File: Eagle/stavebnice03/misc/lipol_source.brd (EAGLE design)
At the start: 24 parts

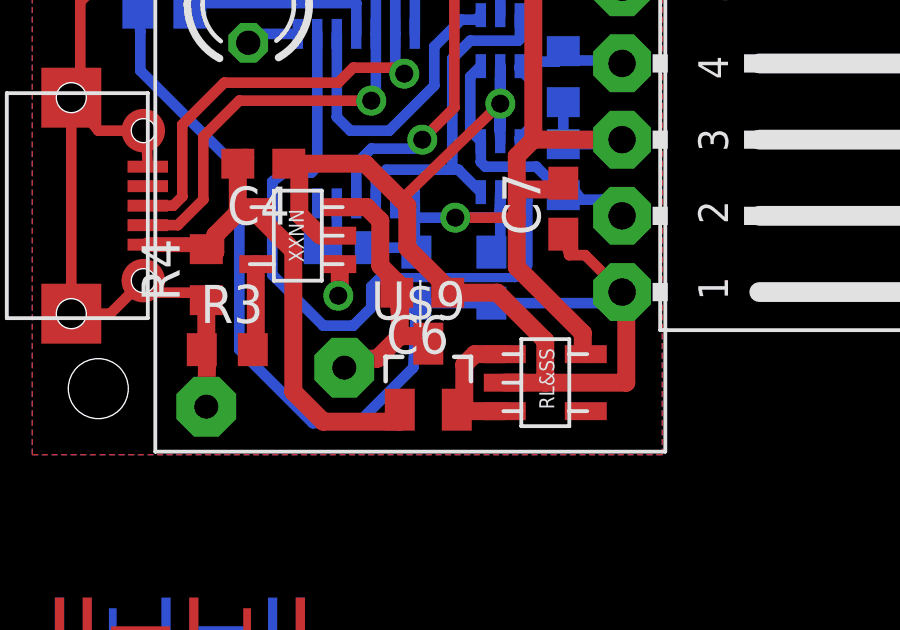
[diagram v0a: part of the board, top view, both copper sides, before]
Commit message: values for lipol charger
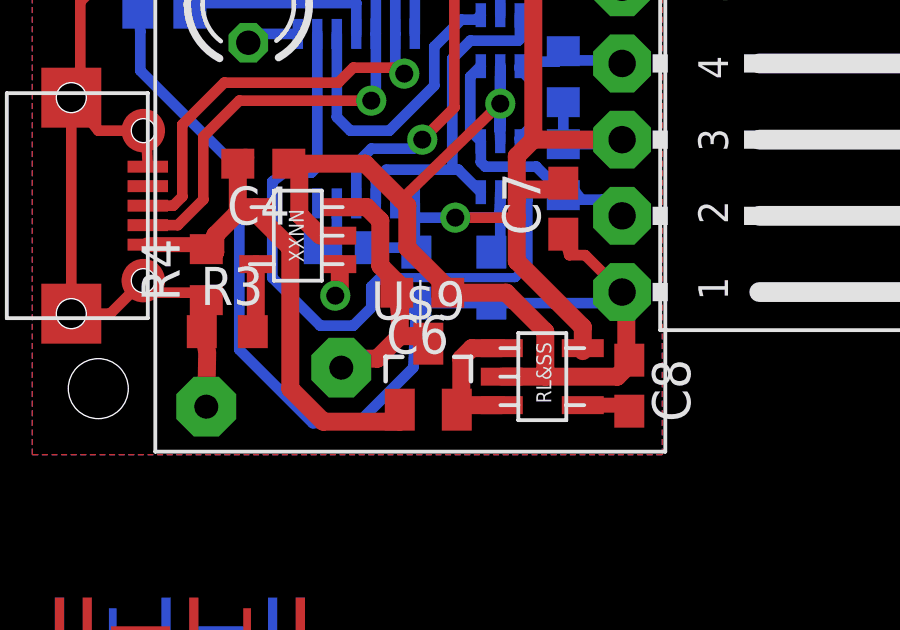
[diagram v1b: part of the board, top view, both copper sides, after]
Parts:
- removed U$8: STABILISER_APE8865, !stavebnice03:SOT32-5
- added C8: 470pF, resistor:C0603
- added TC1185: STABILISER_APE8865, !stavebnice03:SOT32-5
- R3: value 2k2 -> 22k
- R4: value 2k2 -> 100k
- R5: value 0 -> 10k
- R6: value 0 -> 100
- moved R3 0.60 mm to (6.50, 4.10)
- renumbered U$4 to MCP73832, U$6 to NC7SB3157P6X(1), U$7 to NC7SB3157P6X(2)
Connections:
- new net N$17: C8.2, TC1185.BP
- net GND: now also C8.1, TC1185.GND; no longer U$8.GND
- net N$12: now also TC1185.SHDN, TC1185.VIN; no longer U$8.SHDN, U$8.VIN
- net VCC: now also TC1185.VOUT; no longer U$8.VOUT
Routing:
- net N$17: track 0.00 -> 1.75 mm
- net GND: track 138.7 -> 139.3 mm
- net N$11: track 2.89 -> 2.29 mm

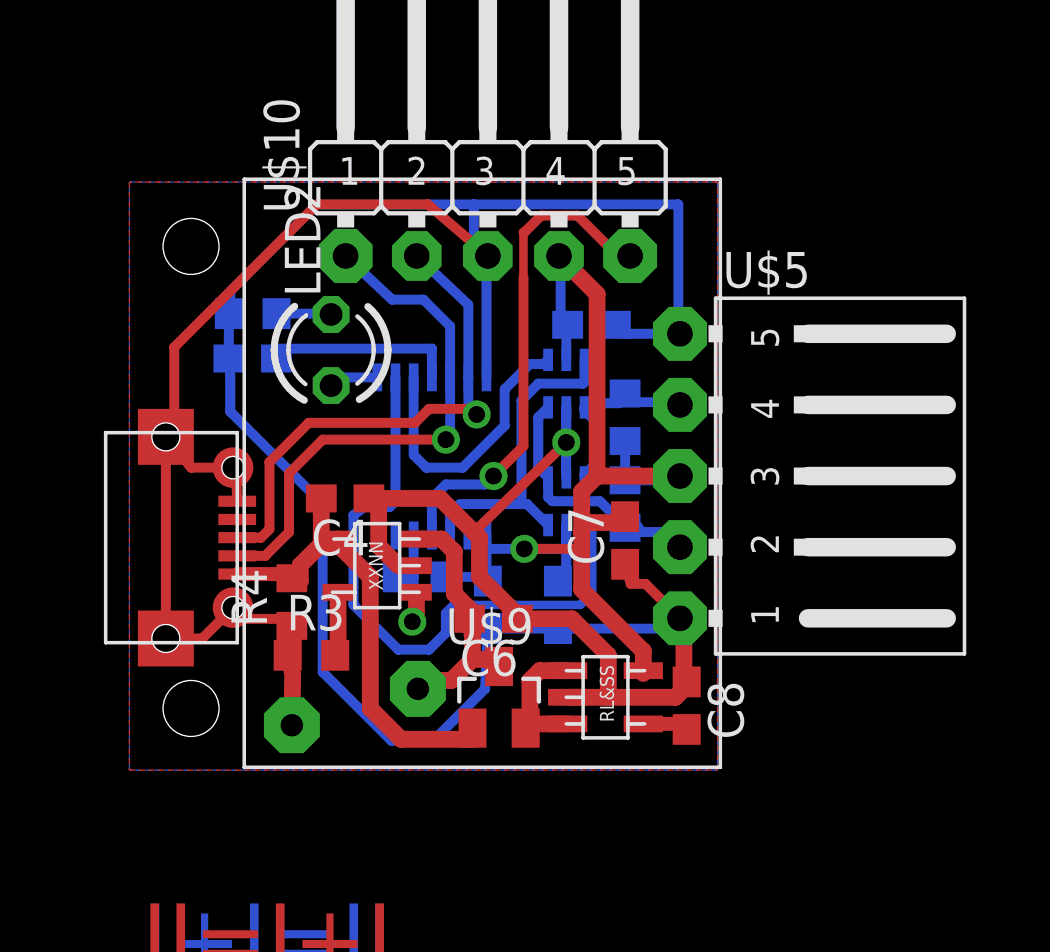
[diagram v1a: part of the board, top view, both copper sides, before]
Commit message: base and battery module size increeased to 22x22
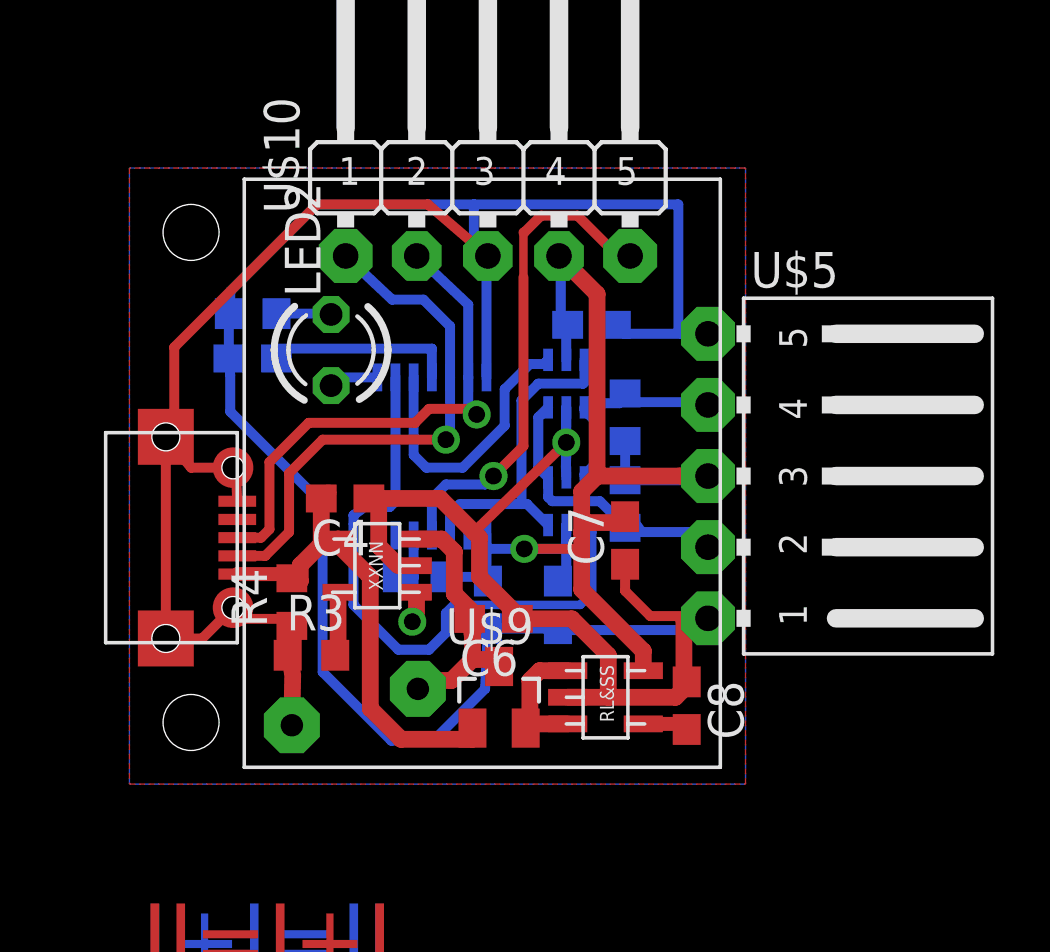
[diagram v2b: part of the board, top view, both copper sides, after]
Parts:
- moved U$5 1.00 mm to (23.2, 10.5)
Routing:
- net GND: track 139.3 -> 144.3 mm
- net VCC: track 40.4 -> 42.1 mm
- net N$6: track 9.27 -> 10.3 mm
- net N$10: track 6.66 -> 7.65 mm

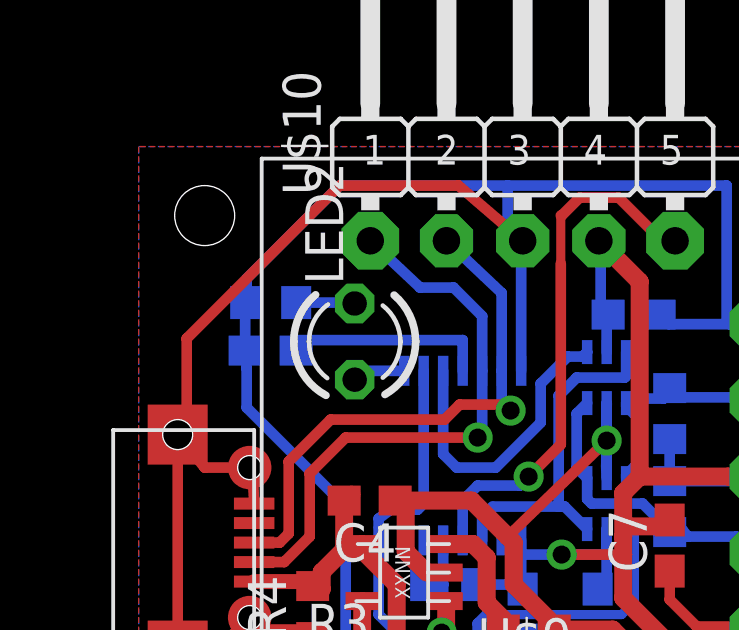
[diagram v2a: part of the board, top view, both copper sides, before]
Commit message: LED resistor increased to a size 0805
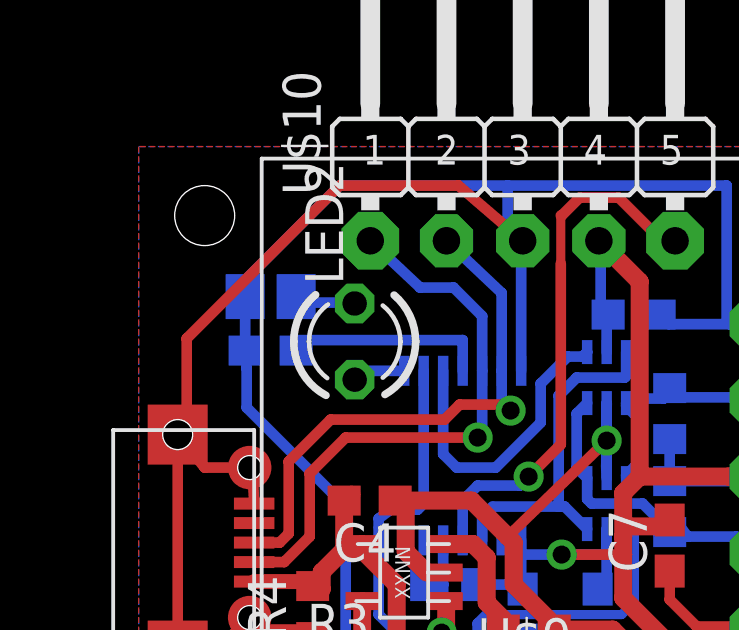
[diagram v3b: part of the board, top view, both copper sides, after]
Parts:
- R6: device resistor:R0603 -> resistor:R0805
- moved R6 0.20 mm to (4.40, 16.5)
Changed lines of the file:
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@@
 <element name="U$10" library="!stavebnice03" package="JUMPER5M-90" value="JUMPER5M-90" x="12.8" y="20.9"/>
 <element name="R5" library="resistor" package="R0603" value="10k" x="10.4" y="6.9" rot="MR0"/>
-<element name="R6" library="resistor" package="R0603" value="100" x="4.4" y="16.3" rot="MR180"/>
+<element name="R6" library="resistor" package="R0805" value="100" x="4.4" y="16.5" rot="MR180"/>
 <element name="LED2" library="led" package="LED3MM" value="" x="7.2" y="15" rot="R90"/>
 <element name="C8" library="resistor" package="C0603" value="470pF" x="19.9" y="2.3" rot="R270"/>
@@
 <wire x1="15.5875" y1="10.7875" x2="15.6" y2="11.7" width="0.357" layer="16"/>
 <via x="15.6" y="11.7" extent="1-16" drill="0.6"/>
-<polygon width="0.01" layer="16" isolate="0.4064" thermals="no" rank="2">
+<polygon width="0.01" layer="16" isolate="0.41" thermals="no" rank="2">
 <vertex x="0" y="-0.5"/>
 <vertex x="0" y="21.5"/>
@@
 <wire x1="15.6" y1="11.7" x2="12.3" y2="8.5" width="0.3556" layer="1"/>
 <contactref element="R6" pad="1"/>
-<wire x1="3.55" y1="14.7" x2="3.55" y2="16.3" width="0.3556" layer="16"/>
+<wire x1="3.55" y1="14.7" x2="3.55" y2="16.5" width="0.3556" layer="16"/>
 <wire x1="1.4" y1="12.4" x2="1.6" y2="12.4" width="0.3556" layer="1"/>
 <wire x1="1.6" y1="12.4" x2="1.6" y2="15.1" width="0.3556" layer="1"/>
@@
 <wire x1="6.7" y1="20.2" x2="3.6" y2="17.1" width="0.3556" layer="16"/>
 <wire x1="3.6" y1="17.1" x2="3.6" y2="16.35" width="0.3556" layer="16"/>
-<wire x1="3.6" y1="16.35" x2="3.55" y2="16.3" width="0.3556" layer="16"/>
+<wire x1="3.6" y1="16.35" x2="3.55" y2="16.5" width="0.3556" layer="16"/>
 <contactref element="C8" pad="1"/>
 <wire x1="15.3" y1="5.05" x2="15.35" y2="5" width="0.3556" layer="16"/>
@@
 <contactref element="R6" pad="2"/>
 <contactref element="LED2" pad="K"/>
-<wire x1="5.25" y1="16.3" x2="6.97" y2="16.3" width="0.3556" layer="16"/>
+<wire x1="5.25" y1="16.5" x2="5.4" y2="16.4" width="0.3556" layer="16"/>
+<wire x1="5.4" y1="16.4" x2="5.5" y2="16.3" width="0.3556" layer="16"/>
+<wire x1="5.5" y1="16.3" x2="6.97" y2="16.3" width="0.3556" layer="16"/>
 <wire x1="6.97" y1="16.3" x2="7.2" y2="16.27" width="0.3556" layer="16"/>
 </signal>

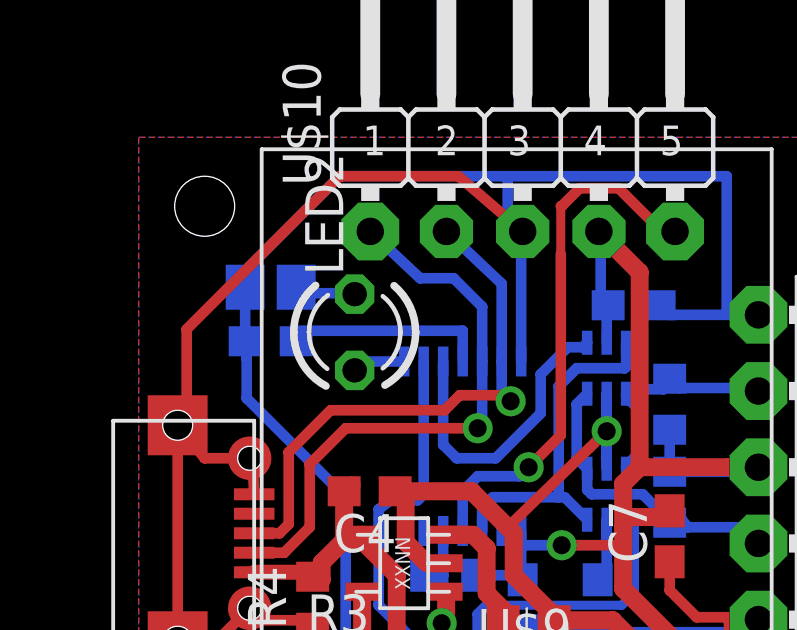
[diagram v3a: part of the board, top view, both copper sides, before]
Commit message: adjutet elemet values
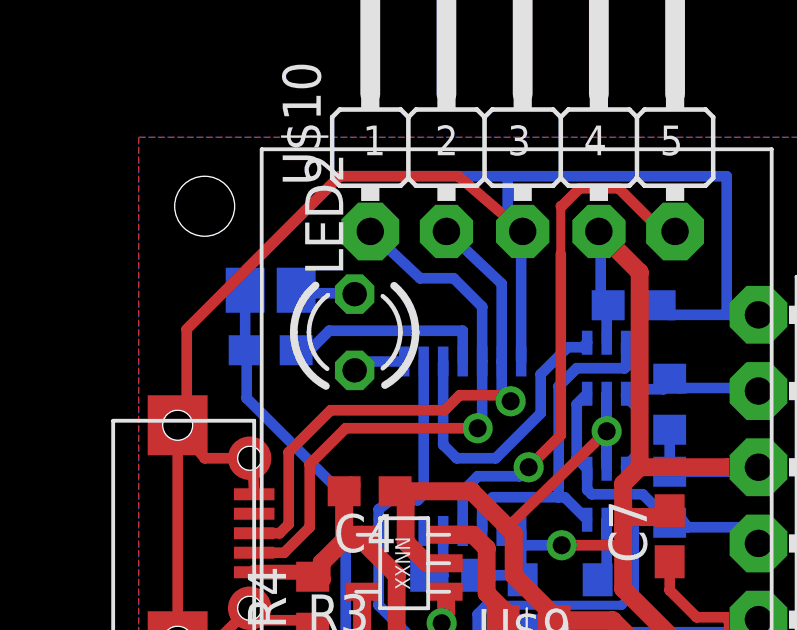
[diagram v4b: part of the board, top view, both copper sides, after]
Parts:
- C7: value 1uF -> 4,7uF
- moved C1 0.30 mm to (4.40, 14.4)
- moved R6 0.10 mm to (4.40, 16.4)
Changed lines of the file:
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@@
 <element name="C5" library="resistor" package="C0603" value="100nF" x="15.3" y="5.9" rot="MR90"/>
 <element name="U$2" library="!stavebnice03" package="MICROUSB-MOLEX" value="USBMICRO" x="1.5" y="8.3" rot="R270"/>
-<element name="C1" library="resistor" package="C0603" value="100nF" x="4.4" y="14.7" rot="MR0"/>
+<element name="C1" library="resistor" package="C0603" value="100nF" x="4.4" y="14.4" rot="MR0"/>
 <element name="U$3" library="!stavebnice03" package="LIPOL_21X17" value="LIPOL_21X17" x="12.1" y="11.1" rot="R180"/>
 <element name="MCP73832" library="!stavebnice03" package="SOT23-5" value="MCP73831" x="8.8" y="7.3" rot="R90"/>
@@
 <element name="U$9" library="!stavebnice03" package="SOT23" value="P-MOSFET-FDV304P" x="13.2" y="2.6"/>
 <element name="R4" library="resistor" package="R0603" value="100k" x="5.8" y="6" rot="R90"/>
-<element name="C7" library="resistor" package="C0603" value="1uF" x="17.7" y="8.2" rot="R90"/>
+<element name="C7" library="resistor" package="C0603" value="4,7uF" x="17.7" y="8.2" rot="R90"/>
 <element name="U$10" library="!stavebnice03" package="JUMPER5M-90" value="JUMPER5M-90" x="12.8" y="20.9"/>
 <element name="R5" library="resistor" package="R0603" value="10k" x="10.4" y="6.9" rot="MR0"/>
-<element name="R6" library="resistor" package="R0805" value="100" x="4.4" y="16.5" rot="MR180"/>
+<element name="R6" library="resistor" package="R0805" value="100" x="4.4" y="16.4" rot="MR180"/>
 <element name="LED2" library="led" package="LED3MM" value="" x="7.2" y="15" rot="R90"/>
 <element name="C8" library="resistor" package="C0603" value="470pF" x="19.9" y="2.3" rot="R270"/>
@@
 <wire x1="19.6" y1="20.2" x2="12.3" y2="20.2" width="0.3556" layer="16"/>
 <wire x1="12.3" y1="20.2" x2="6.7" y2="20.2" width="0.3556" layer="16"/>
-<wire x1="3.55" y1="14.7" x2="3.6" y2="14.1" width="0.3556" layer="16"/>
+<wire x1="3.55" y1="14.4" x2="3.6" y2="14.1" width="0.3556" layer="16"/>
 <wire x1="12.75" y1="14.025" x2="12.75" y2="17.95" width="0.3556" layer="16"/>
 <wire x1="12.75" y1="17.95" x2="12.7" y2="18.2" width="0.3556" layer="16"/>
@@
 <wire x1="15.6" y1="11.7" x2="12.3" y2="8.5" width="0.3556" layer="1"/>
 <contactref element="R6" pad="1"/>
-<wire x1="3.55" y1="14.7" x2="3.55" y2="16.5" width="0.3556" layer="16"/>
+<wire x1="3.55" y1="14.4" x2="3.55" y2="16.4" width="0.3556" layer="16"/>
 <wire x1="1.4" y1="12.4" x2="1.6" y2="12.4" width="0.3556" layer="1"/>
 <wire x1="1.6" y1="12.4" x2="1.6" y2="15.1" width="0.3556" layer="1"/>
@@
 <wire x1="6.7" y1="20.2" x2="3.6" y2="17.1" width="0.3556" layer="16"/>
 <wire x1="3.6" y1="17.1" x2="3.6" y2="16.35" width="0.3556" layer="16"/>
-<wire x1="3.6" y1="16.35" x2="3.55" y2="16.5" width="0.3556" layer="16"/>
+<wire x1="3.6" y1="16.35" x2="3.55" y2="16.4" width="0.3556" layer="16"/>
 <contactref element="C8" pad="1"/>
 <wire x1="15.3" y1="5.05" x2="15.35" y2="5" width="0.3556" layer="16"/>
@@
 <contactref element="C1" pad="1"/>
 <wire x1="10.8" y1="14.025" x2="10.8" y2="15.05" width="0.3556" layer="16"/>
-<wire x1="10.8" y1="15.05" x2="5.2" y2="15.05" width="0.3556" layer="16"/>
-<wire x1="5.2" y1="15.05" x2="5.25" y2="14.7" width="0.3556" layer="16"/>
+<wire x1="10.8" y1="15.05" x2="6.35" y2="15.05" width="0.3556" layer="16"/>
+<wire x1="6.35" y1="15.05" x2="5.8" y2="14.5" width="0.3556" layer="16"/>
+<wire x1="5.8" y1="14.5" x2="5.35" y2="14.5" width="0.3556" layer="16"/>
+<wire x1="5.35" y1="14.5" x2="5.25" y2="14.4" width="0.3556" layer="16"/>
 </signal>
 <signal name="N$4">
@@
 <contactref element="R6" pad="2"/>
 <contactref element="LED2" pad="K"/>
-<wire x1="5.25" y1="16.5" x2="5.4" y2="16.4" width="0.3556" layer="16"/>
+<wire x1="5.25" y1="16.4" x2="5.4" y2="16.4" width="0.3556" layer="16"/>
 <wire x1="5.4" y1="16.4" x2="5.5" y2="16.3" width="0.3556" layer="16"/>
 <wire x1="5.5" y1="16.3" x2="6.97" y2="16.3" width="0.3556" layer="16"/>
